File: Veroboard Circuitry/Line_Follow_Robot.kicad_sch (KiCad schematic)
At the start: 40 parts, among them J1 GPIOA (TBC), J2 GPIOB (TBC), J3 GPIOC (TBC), J4 PB1, J5 PB2, SW1 SW_Push, SW2 SW_Push, U1 LM317T, U2 LM741, U3 LM358, U4 LM317T, U5 LM741, U6 LM358

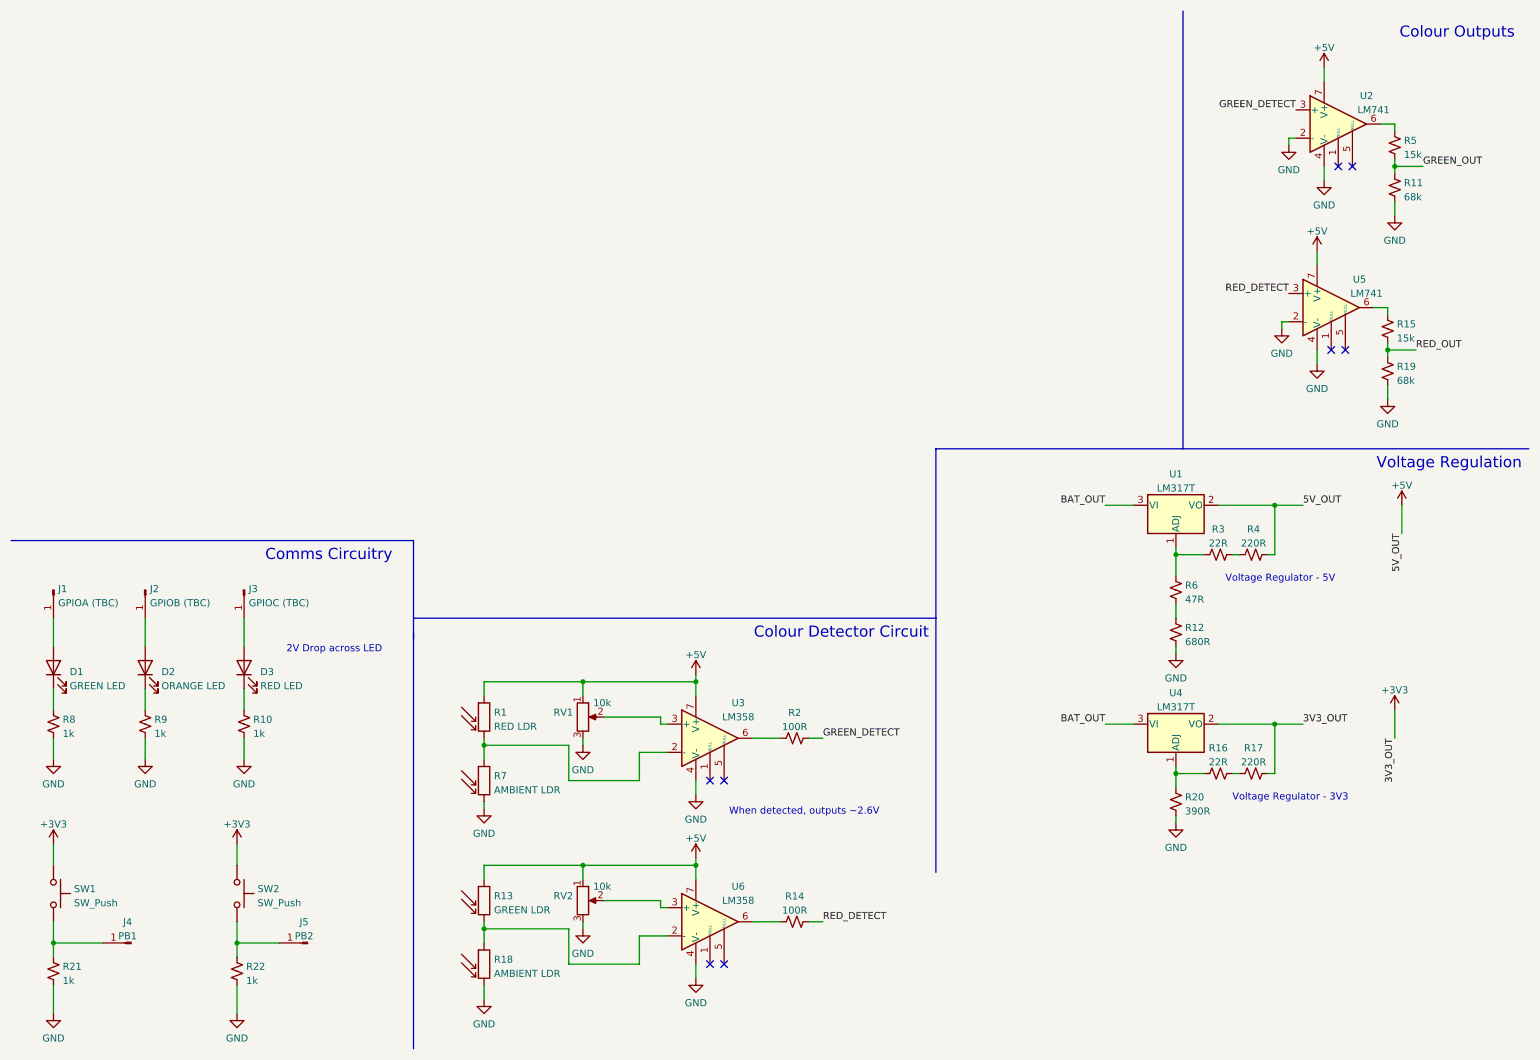
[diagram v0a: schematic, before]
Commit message: Upload BOM v0.1
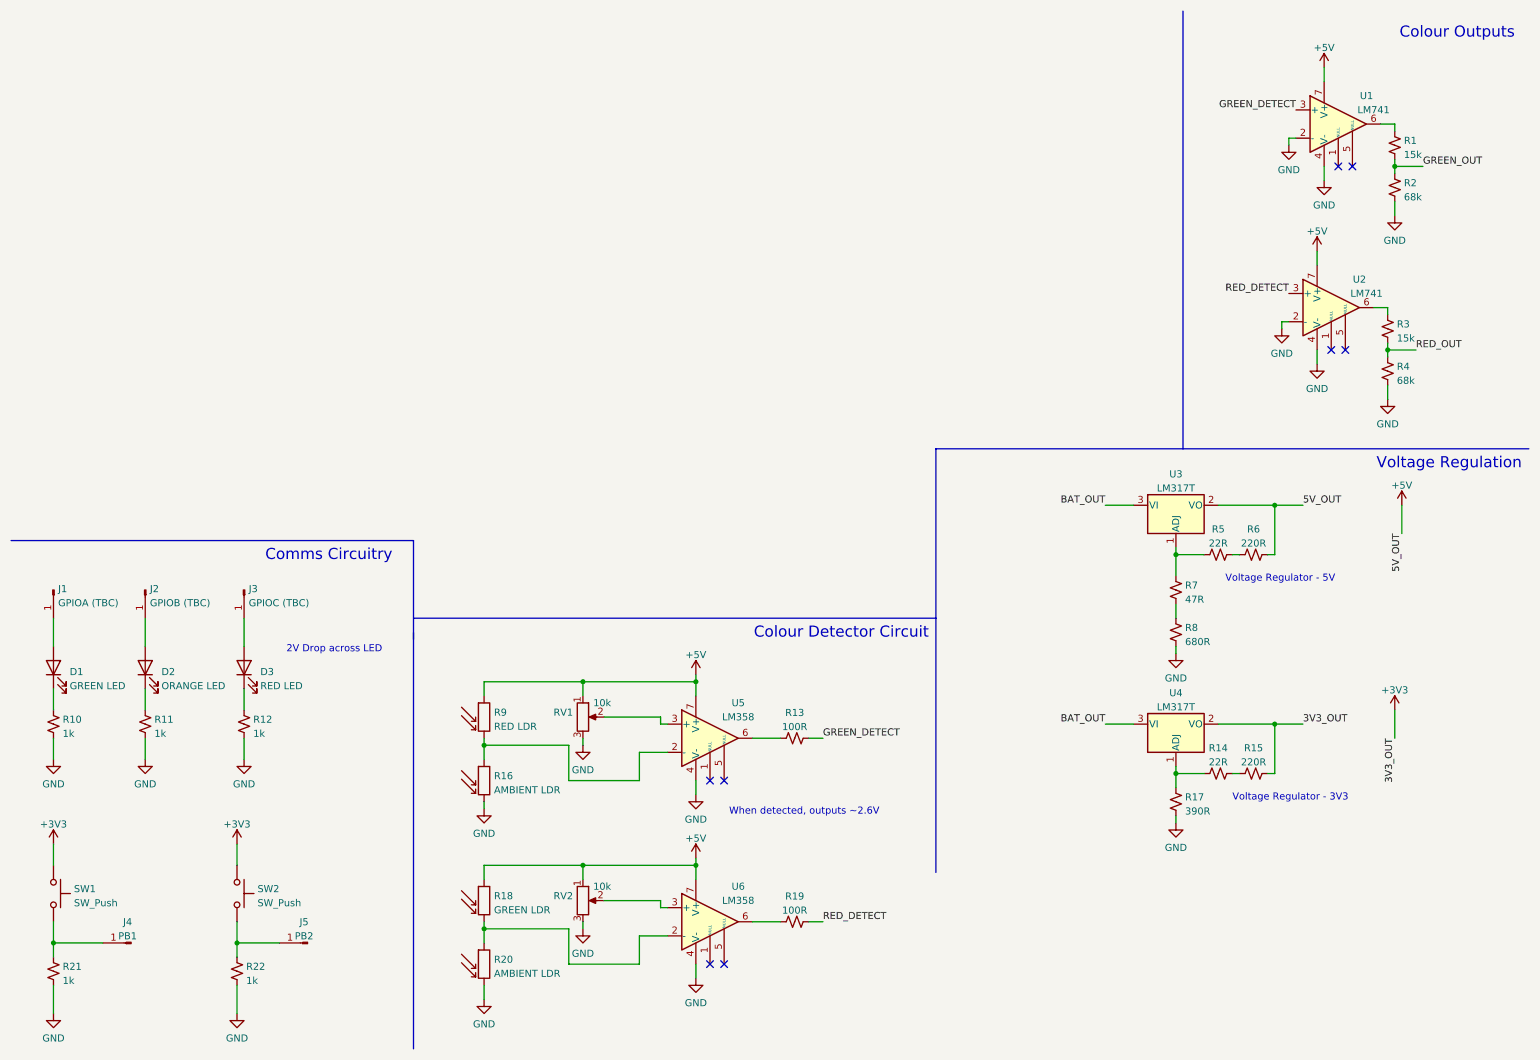
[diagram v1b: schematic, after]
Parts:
- renumbered R5 to R1, R8 to R10, R9 to R11, R10 to R12, R2 to R13, R16 to R14, R17 to R15, R7 to R16, R20 to R17, R13 to R18, R14 to R19, R11 to R2, R18 to R20, R15 to R3, R19 to R4, R3 to R5, R4 to R6, R6 to R7, R12 to R8, R1 to R9, U2 to U1, U5 to U2, U1 to U3, U3 to U5
